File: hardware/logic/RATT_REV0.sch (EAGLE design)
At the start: 128 parts, among them IC1 TLP292-4, IC13 MCP73832, IC16 PCA9539PW, IC2 CPC1002N, IC200 TPS2115AIPWRQ1, IC3 CPC1002N, IC300 MAX98357, IC4 CPC1002N, IC5 CPC1002N, IC500 AP2112K-3.3V, J1 4P-2.0, J100 PHOENIX1803426, J2 4P-2.0, J4 4P-2.0, J5 F-1X04-SIP-100-40, J6 4P-2.0, J7 PHOENIX1803484, J8 PHOENIX1803484, J87 RPI-ZERO, Q5 2N7002

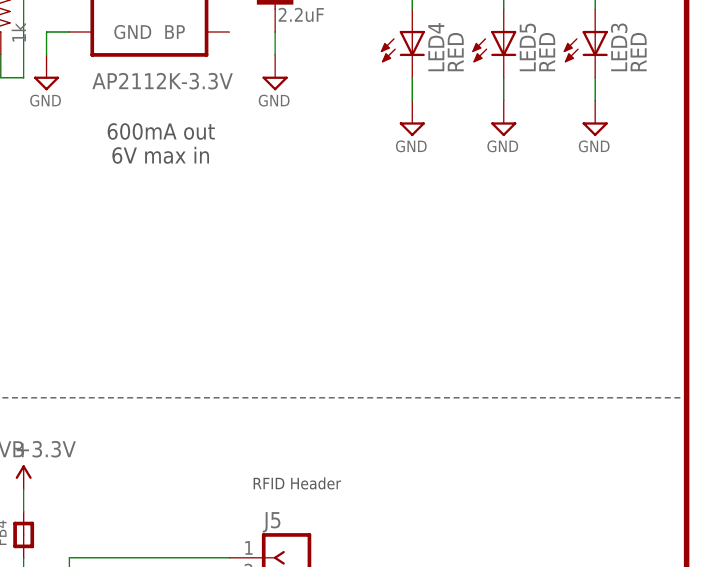
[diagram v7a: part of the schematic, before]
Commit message: Added Test Points, GND Vias
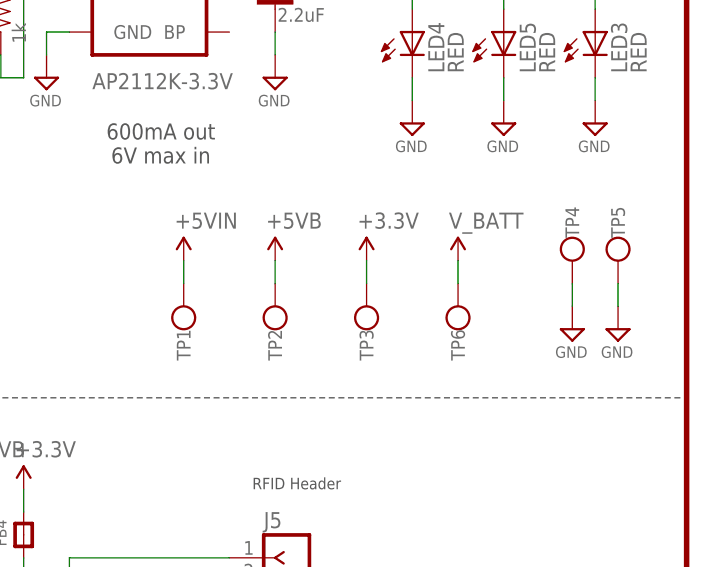
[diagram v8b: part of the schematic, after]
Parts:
- added TP1: 5VIN, MakeItLabs:RCW-0C
- added TP2: 5VB, MakeItLabs:RCW-0C
- added TP3: 3.3V, MakeItLabs:RCW-0C
- added TP4, TP5: GND, MakeItLabs:RCW-0C
- added TP6: BATT, MakeItLabs:RCW-0C
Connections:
- net +3.3V: now also TP3.TP
- net +5VB: now also TP2.TP
- net +5VIN: now also TP1.TP
- net GND: now also TP4.TP, TP5.TP
- net V_BATT: now also TP6.TP
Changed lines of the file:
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@@
 <setting verticaltext="up"/>
 </settings>
-<grid distance="0.1" unitdist="inch" unit="inch" style="lines" multiple="1" display="no" altdistance="0.01" altunitdist="inch" altunit="inch"/>
+<grid distance="0.1" unitdist="inch" unit="inch" style="lines" multiple="1" display="yes" altdistance="0.01" altunitdist="inch" altunit="inch"/>
 <layers>
 <layer number="1" name="Top" color="4" fill="1" visible="no" active="no"/>
@@
 <part name="SUPPLY95" library="MakeItLabs" deviceset="+5VIN" device=""/>
 <part name="SUPPLY96" library="MakeItLabs" deviceset="+3.3V" device=""/>
+<part name="TP1" library="MakeItLabs" deviceset="RCW-0C" device="" value="5VIN"/>
+<part name="TP2" library="MakeItLabs" deviceset="RCW-0C" device="" value="5VB"/>
+<part name="TP3" library="MakeItLabs" deviceset="RCW-0C" device="" value="3.3V"/>
+<part name="TP4" library="MakeItLabs" deviceset="RCW-0C" device="" value="GND"/>
+<part name="TP5" library="MakeItLabs" deviceset="RCW-0C" device="" value="GND"/>
+<part name="SUPPLY61" library="MakeItLabs" deviceset="GND" device=""/>
+<part name="SUPPLY68" library="MakeItLabs" deviceset="GND" device=""/>
+<part name="SUPPLY91" library="MakeItLabs" deviceset="+5VIN" device=""/>
+<part name="SUPPLY97" library="MakeItLabs" deviceset="+5VB" device=""/>
+<part name="SUPPLY98" library="MakeItLabs" deviceset="+3.3V" device=""/>
+<part name="SUPPLY99" library="MakeItLabs" deviceset="V_BATT" device=""/>
+<part name="TP6" library="MakeItLabs" deviceset="RCW-0C" device="" value="BATT"/>
 </parts>
 <sheets>
@@
 </instance>
 <instance part="SUPPLY96" gate="G$1" x="292.1" y="35.56"/>
+<instance part="TP1" gate="G$1" x="375.92" y="205.74" smashed="yes" rot="R270">
+<attribute name="NAME" x="375.92" y="203.2" size="1.524" layer="95" font="vector" rot="R270" align="center-left"/>
+</instance>
+<instance part="TP2" gate="G$1" x="386.08" y="205.74" smashed="yes" rot="R270">
+<attribute name="NAME" x="386.08" y="203.2" size="1.524" layer="95" font="vector" rot="R270" align="center-left"/>
+</instance>
+<instance part="TP3" gate="G$1" x="396.24" y="205.74" smashed="yes" rot="R270">
+<attribute name="NAME" x="396.24" y="203.2" size="1.524" layer="95" font="vector" rot="R270" align="center-left"/>
+</instance>
+<instance part="TP4" gate="G$1" x="419.1" y="210.82" smashed="yes" rot="R90">
+<attribute name="NAME" x="419.1" y="213.36" size="1.524" layer="95" font="vector" rot="R90" align="center-left"/>
+</instance>
+<instance part="TP5" gate="G$1" x="424.18" y="210.82" smashed="yes" rot="R90">
+<attribute name="NAME" x="424.18" y="213.36" size="1.524" layer="95" font="vector" rot="R90" align="center-left"/>
+</instance>
+<instance part="SUPPLY61" gate="GND" x="424.18" y="203.2" smashed="yes">
+<attribute name="VALUE" x="422.275" y="200.025" size="1.27" layer="96" font="vector"/>
+</instance>
+<instance part="SUPPLY68" gate="GND" x="419.1" y="203.2" smashed="yes">
+<attribute name="VALUE" x="417.195" y="200.025" size="1.27" layer="96" font="vector"/>
+</instance>
+<instance part="SUPPLY91" gate="G$1" x="375.92" y="210.82"/>
+<instance part="SUPPLY97" gate="G$1" x="386.08" y="210.82"/>
+<instance part="SUPPLY98" gate="G$1" x="396.24" y="210.82"/>
+<instance part="SUPPLY99" gate="G$2" x="406.4" y="210.82"/>
+<instance part="TP6" gate="G$1" x="406.4" y="205.74" smashed="yes" rot="R270">
+<attribute name="NAME" x="406.4" y="203.2" size="1.524" layer="95" font="vector" rot="R270" align="center-left"/>
+</instance>
 </instances>
 <busses>
@@
 <pinref part="J3" gate="A" pin="6"/>
 </segment>
+<segment>
+<pinref part="TP5" gate="G$1" pin="TP"/>
+<pinref part="SUPPLY61" gate="GND" pin="GND"/>
+<wire x1="424.18" y1="205.74" x2="424.18" y2="208.28" width="0.1524" layer="91"/>
+</segment>
+<segment>
+<pinref part="TP4" gate="G$1" pin="TP"/>
+<pinref part="SUPPLY68" gate="GND" pin="GND"/>
+<wire x1="419.1" y1="205.74" x2="419.1" y2="208.28" width="0.1524" layer="91"/>
+</segment>
 </net>
 <net name="N$1" class="0">
@@
 <pinref part="SUPPLY63" gate="G$2" pin="V_BATT"/>
 </segment>
+<segment>
+<pinref part="SUPPLY99" gate="G$2" pin="V_BATT"/>
+<pinref part="TP6" gate="G$1" pin="TP"/>
+<wire x1="406.4" y1="208.28" x2="406.4" y2="210.82" width="0.1524" layer="91"/>
+</segment>
 </net>
 <net name="N$11" class="0">
@@
 <pinref part="J3" gate="A" pin="4"/>
 </segment>
+<segment>
+<pinref part="TP1" gate="G$1" pin="TP"/>
+<pinref part="SUPPLY91" gate="G$1" pin="+5VIN"/>
+<wire x1="375.92" y1="208.28" x2="375.92" y2="210.82" width="0.1524" layer="91"/>
+</segment>
 </net>
 <net name="+5VB" class="0">
@@
 <junction x="144.78" y="231.14"/>
 </segment>
+<segment>
+<pinref part="TP2" gate="G$1" pin="TP"/>
+<pinref part="SUPPLY97" gate="G$1" pin="+5VB"/>
+<wire x1="386.08" y1="208.28" x2="386.08" y2="210.82" width="0.1524" layer="91"/>
+</segment>
 </net>
 <net name="+3.3V" class="0">
@@
 <pinref part="J3" gate="A" pin="8"/>
 </segment>
+<segment>
+<pinref part="TP3" gate="G$1" pin="TP"/>
+<pinref part="SUPPLY98" gate="G$1" pin="+3.3V"/>
+<wire x1="396.24" y1="208.28" x2="396.24" y2="210.82" width="0.1524" layer="91"/>
+</segment>
 </net>
